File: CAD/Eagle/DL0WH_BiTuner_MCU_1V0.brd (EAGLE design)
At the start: 96.5 x 96.5 mm, 526 parts, among them Q0321 ABS07-32.768KHZ, Q1321 ABS07-32.768KHZ, Q2211 ABM3B-32.0000MHZ, Q2311 ABM3B-16.0000MHZ, T1051 MMBT2222, T1111 MMBT2222, T1121 MMBT2222, T1131 MMBT2222, U0111 STM32L4Z_144PIN_SMPS, U0521 PCAL6416APW, U0621 PCAL6416APW, U0711 IS25LP032D, U0721 IS25LP032D, U0801 CAT24C64, U0911 ZIO_EINK_1IN54, U1001 MIDAS_MCCOG21605B6W-FPTLWI, U1301 BNO085, U1401 BME680, U1501 LM4120IM5-3.0, U1511 MAX5217, U1531 CFPT-141-20MHZ, U1541 OPA354, U1542 LPV811, U1601 Si5338, U1651 TS5A23166, U1701 PCM1863, U1801 WM8523, U1901 SIM868, U2001 74LVC4245A, U2101 74LVC4245A, U2201 SX1262, U2271 PE4259, U2301 AX5243, U2401 LM53603-Q1, U2501 BQ24193, U2541 LPV811, U2601 BQ25570, U2681 TS5A23166, U2701 TPS62051, U2751 MCP4661-104E-MS, U2801 TS5A23166, U2901 TS5A23166, U3001 TS5A23166, U3101 TS5A23166, U3391 TS5A23166, U3392 TDK B4310, X1201 TTE_EN11-HSM, X1951 MICROSIM-8P_SDCARD-8P_MOLEX-1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, X2411 WIRE-TO-BOARD_5MM08_1X02, X2551 JST_S3B-XH-A, X2601 WIRE-TO-BOARD_5MM08_1X02, X3201 MOLEX 105017-0001, X3301 SMA_SMT_AMPHENOL-901-143, X3311 SAMTEC SMA-J-P-H-RA-TH1, X3371 SMA_SMT_AMPHENOL-901-143, SAM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, X3381 SMA_SMT_AMPHENOL-901-143, SAM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, X3391 SMA_SMT_AMPHENOL-901-143, SAM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, X3401 CUI SJ1-3535NS, X3411 CUI SJ1-3535NS, X3511 2X20/90_1MM27_HARWIN_M50-3202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, X3512 2X20/90_1MM27_HARWIN_M50-3202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, X3531 2X20/90_1MM27_HARWIN_M50-3202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, X3532 2X20/90_1MM27_HARWIN_M50-3202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

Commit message: HW_1V0 - CAD/Eagle - Initial setup of new PCB
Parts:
- removed C0404, C0405, C0406, C0407, C0408, C0409, C0421, C0422, C0441, C0621, C0901, C1001, C1101, C1301, C1302, C1303, C1401, C1501, C1511, C1512, C1531, C1541, C1543, C1602, C1603, C1605, C1702, C1703, C1705, C1902, C2101, C2202, C2271, C2301, C2302, C2303, C2541, C2602, C2702, C2751, C2801, C2802, C2803, C2901, C2902, C2903, C3001, C3002, C3003, C3101, C3102, C3103, C3104, C3105, C3393: 100nF, df4iah_rcl:C0402
- removed C0423, C1801, C1802, C2606: 4.7uF, df4iah_rcl:C0402
- removed C0442, C1011, C1012, C1522, C1811, C1812, C1961, C2502, C2521: 1uF, df4iah_rcl:C0402
- removed C0711, C0721, C0801, C1601, C1604, C1951, C1955: 220nF, df4iah_rcl:C0402
- removed C1201, C1202, C1203, C1542, C2272: 1nF, df4iah_rcl:C0402
- removed C1321, C1322, C1952, C1953, C1954: 22pF, df4iah_rcl:C0402
- removed C1532: 100pF, df4iah_rcl:C0402
- removed C1615, C1616, C1712, C1722, C1903, C2603, C2605, C2653: 10nF, df4iah_rcl:C0402
- removed C1701, C1704, C1711, C1721, C1904, C2201, C2501, C2504, C2505, C2511, C2601, C2652, C2701: 10uF, df4iah_rcl:C0402
- removed C1706, C1803: 2.2uF, df4iah_rcl:C0402
- removed C1831, C1841: 2.7nF, df4iah_rcl:C0402
- removed C1901, C2204: 47pF, df4iah_rcl:C0402
- removed C2203: 470nF, df4iah_rcl:C0402
- removed C2205, C2503: 47nF, df4iah_rcl:C0402
- removed C2263, C2282, C2283: 3.3pF, df4iah_rcl:C0402
- removed C2264, C2281: 39pF, df4iah_rcl:C0402
- removed C2265, C2293, C3371, C3372, C3381, C3382, C3391, C3392: 0pF, df4iah_rcl:C0402
- removed C2266: 5.6pF, df4iah_rcl:C0402
- removed C2267: 2.2pF, df4iah_rcl:C0402
- removed C2291, C3386: 1.8pF, df4iah_rcl:C0402
- removed C2292: 2.4pF, df4iah_rcl:C0402
- removed C2312, C2313, C2316: N/A, df4iah_rcl:C0402
- removed C2314, C2315: 4.3pF, df4iah_rcl:C0402
- removed C2317, C2318, C2321, C2322, C2323: 4.7pF, df4iah_rcl:C0402
- removed C2682: 1F_6V_SCMR18H105MRBB0, df4iah_rcl:C115-080X160_POL
- removed C2703: 22uF, df4iah_rcl:C0402
- removed C2791: 6.8pF, df4iah_rcl:C0402
- removed C3383: 0.5pF, df4iah_rcl:C0402
- removed C3385, C3389: 1.2pF, df4iah_rcl:C0402
- removed C3388: 1.5pF, df4iah_rcl:C0402
- removed D1101: ASMT-YTB7-0AA02_RGB, df4iah_led:ASMT-YTB7_0AA02_RGB
- removed D1901: CMAD6001, df4iah_diode:SOD923
- removed D1902: MMSZ4690-E3-08 (5.6V), df4iah_diode:SOD123
- removed D2521, D2681, D2801, D2802: CRS08, df4iah_diode:SOD80C
- removed FM1, FM2, FM3: (no value), df4iah_fiducial:FIDUCIAL_MARK_1MM
- removed L1701, L1801: 10uH, df4iah_rcl:L0603
- removed L2201: 15uH, df4iah_rcl:L_3.00MM_X_3.00MM
- removed L2261: 0R, df4iah_rcl:L0603
- removed L2262: 47nH, df4iah_rcl:L0603
- removed L2263: 2.5nH, df4iah_rcl:L0603
- removed L2264, L3386, L3388: 4.7nH, df4iah_rcl:L0603
- removed L2282: 9.1nH, df4iah_rcl:L0603
- removed L2291: 15nH, df4iah_rcl:L0603
- removed L2311, L2316, L2317, L2321: 22nH, df4iah_rcl:L0603
- removed L2312, L2313: 100nH, df4iah_rcl:L0603
- removed L2314, L2315: 43nH, df4iah_rcl:L0603
- removed L2501: 2.2uH, df4iah_rcl:L_6.00MM_X_6.00MM
- removed L2601: 22uH, df4iah_rcl:WE-TPC_3MM8-3MM8_R-1MM3
- removed L2651, L2791: 10uH, df4iah_rcl:L_4.90MM_X_4.90MM
- removed L3384: 1.2nH, df4iah_rcl:L0603
- removed L3387: 2.7nH, df4iah_rcl:L0603
- removed L3393: WE-CBF_300R, rcl:L3216C
- removed Q1321: ABS07-32.768KHZ, df4iah_crystal:ABS07
- removed Q2211: ABM3B-32.0000MHZ, df4iah_crystal:ABM3B
- removed Q2311: ABM3B-16.0000MHZ, df4iah_crystal:ABM3B
- removed R0531, R0631, R0901, R0902, R0903, R0904, R1301, R1302, R1303, R1304, R1538, R1539, R1541, R1623, R1631, R1632, R1643, R1644, R1651, R1751, R1752, R1753, R1761, R1821, R1822, R1823, R1824, R1951, R1952, R1953, R2110, R2111, R2112, R2113, R2120, R2121, R2122, R2123, R2211, R2221, R2222, R2223, R2224, R2251, R2252, R2253, R2321, R2341, R2351, R2391, R2554, R2811, R3501, R3502, R3503, R3504, R3505, R3506, R3507, R3508, R3509, R3510, R3511, R3514, R3515, R3516, R3517, R3518, R3519, R3520, R3521, R3522, R3523, R3566, R3567, R3568, R3569, R3570, R3571, R3572, R3573, R3574, R3575, R3576, R3579, R3580, R3581, R3582, R3583, R3584, R3585, R3586, R3587, R3588: 47R, df4iah_rcl:R0402
- removed R0581, R0591, R0681, R0691: 1MR, df4iah_rcl:EXBD
- removed R0621, R1521, R2331, R2332, R2612, R2701, R2711: 100kR, df4iah_rcl:R0402
- removed R0891, R0892, R1811, R1812, R2521, R2651, R2681, R3512, R3513, R3577, R3578: 0R, df4iah_rcl:R0402
- removed R1031: 220kR, df4iah_rcl:R0402
- removed R1051, R1111, R1121, R1131: 1.5kR, df4iah_rcl:R0402
- removed R1052, R1112, R1122, R1132: 2.0kR, df4iah_rcl:R0402
- removed R1053: 27R, df4iah_rcl:R0402
- removed R1113, R1123, R1133: 27R, rcl:R0805
- removed R1331, R1332: 2kR, df4iah_rcl:R0402
- removed R1531, R1711, R1721, R1901, R1942: 10kR, df4iah_rcl:R0402
- removed R1542, R2803, R2804: 1MR, df4iah_rcl:R0402
- removed R1543, R2541: 33kR, df4iah_rcl:R0402
- removed R1611, R1612, R1635, R1636, R1661, R2114, R2115, R2116, R2117, R2124, R2125, R2126, R2127: N/A, df4iah_rcl:R0402
- removed R1712, R1722, R2801, R2802: 100R, df4iah_rcl:R0402
- removed R1731, R1741, R1742, R1743, R1744, R1745, R1746: D.C., df4iah_rcl:R0402
- removed R1831, R1841: 560R, df4iah_rcl:R0402
- removed R1941: NTC 10kR, df4iah_rcl:R0402
- removed R1943, R1944: 4.7kR, df4iah_rcl:R0402
- removed R1961, R1962: 22R, df4iah_rcl:R0402
- removed R2501: 240R, df4iah_rcl:R0402
- removed R2511: 2.27kR, df4iah_rcl:R0402
- removed R2512: 6.86kR, df4iah_rcl:R0402
- removed R2611: 1kR, df4iah_rcl:R0402
- removed R2621, R2633: 1.82MR, df4iah_rcl:R0402
- removed R2622: 10.0MR, df4iah_rcl:R0402
- removed R2631: 3.65MR, df4iah_rcl:R0402
- removed R2632: 7.50MR, df4iah_rcl:R0402
- removed R2641: 4.75MR, df4iah_rcl:R0402
- removed R2642: 8.20MR, df4iah_rcl:R0402
- removed R2712: 150kR, df4iah_rcl:R0402
- removed R3371, R3381, R3391: 0R, df4iah_rcl:R0603
- removed RPOLY3393: 50mA/150mA, rcl:R1210
- removed SJ0121, SJ0421, SJ0422, SJ0423, SJ0424: (no value), df4iah_jumper:SJ
- removed T1051, T1111, T1121, T1131: MMBT2222, transistor:SOT23
- removed TP_+1V1, TP_+1V2_MCU, TP_+3V3_HICUR, TP_+3V3_XO, TP_+3V3_XO_PA, TP_BQ_VBAT, TP_BQ_VOUT, TP_BQ_VSTOR, TP_IN_CLK1, TP_IN_CLK2, TP_LIPO_BAT, TP_LIPO_CUR, TP_LIPO_SYS, TP_VSOL, TP_VUSB_SW: PTR1B1,27, testpad:B1,27
- removed TP_AX_ADC1, TP_AX_ADC2, TP_AX_IRQ, TP_AX_TCXO_EN, TP_SX_DIO1, TP_SX_DIO2, TP_SX_DIO3: PTR1TP06R, testpad:TP06R
- removed U0111: STM32L4Z_144PIN_SMPS, df4iah_stm32l4:LQFP144
- removed U0621: PCAL6416APW, df4iah_dataconvertion:TSSOP24_SOT355-1
- removed U0711, U0721: IS25LP032D, df4iah_memory:SOIC8_150MIL
- removed U0801: CAT24C64, df4iah_memory:SOIC8_150MIL
- removed U0911: ZIO_EINK_1IN54, df4iah_lcd:ZIO_EINK_1IN54
- removed U1001: MIDAS_MCCOG21605B6W-FPTLWI, df4iah_lcd:MIDAS_MCCOG21605B6W-FPTLWI
- removed U1301: BNO085, df4iah_sensors:BNO085_LGA28
- removed U1401: BME680, df4iah_sensors:BME680
- removed U1501: LM4120IM5-3.0, df4iah_powersupply:SOT95P285X120-5N
- removed U1511: MAX5217, df4iah_dac:µMAX8
- removed U1531: CFPT-141-20MHZ, df4iah_osc:CFPT-141
- removed U1541: OPA354, df4iah_opamp:SOT-23-5
- removed U1542, U2541: LPV811, df4iah_opamp:SOT-23-5
- removed U1601: Si5338, df4iah_osc:QFN24_P0MM5_CTRPAD
- removed U1651, U2681, U2801, U2901, U3001, U3101, U3391: TS5A23166, df4iah_sc-switches:R-PDSO-G8
- removed U1701: PCM1863, df4iah_adc:R-PDSO-G30
- removed U1801: WM8523, df4iah_dac:TSSOP20
- removed U1901: SIM868, df4iah_gsm:SIM868
- removed U2101: 74LVC4245A, df4iah_dataconvertion:TSSOP24_SOT355-1
- removed U2201: SX1262, df4iah_rf:QFN24-4X4-0P5-PAD
- removed U2271: PE4259, df4iah_rf:SC-70_6-LEAD_2X1MM25_0P65
- removed U2301: AX5243, df4iah_rf:QFN20-4X4-0P5-PAD
- removed U2501: BQ24193, df4iah_powersupply:VQFN-24
- removed U2601: BQ25570, df4iah_powersupply:V-PVQFN-20
- removed U2701: TPS62051, df4iah_powersupply:S-PDSO-G10
- removed U2751: MCP4661-104E-MS, df4iah_dig-pot:TSSOP14
- removed U3392: TDK B4310, df4iah_rf:QCS5P
- removed X1201: TTE_EN11-HSM, df4iah_switch:TTE_EN11-HSM
- removed X1951: MICROSIM-8P_SDCARD-8P_MOLEX-104642-1610, df4iah_connector:MICROSIM-8P_SDCARD-8P_MOLEX-104642-1610
- removed X1961: (no value), df4iah_connector:2X02
- removed X2551: JST_S3B-XH-A, df4iah_connector:JST_S3B-XH-A
- removed X2601: WIRE-TO-BOARD_5MM08_1X02, df4iah_connector:WIRE-TO-BOARD_5MM08_1X02
- removed X3371, X3381, X3391: SMA_SMT_AMPHENOL-901-143, SAMTEC SMA-J-P-H-RA-TH1, df4iah_connector:SMA_SMT_AMPHENOL_901-143
- removed X3401, X3411: CUI SJ1-3535NS, df4iah_connector:SJ1-353XNS_3MM5-STEREO-AUDIO-JACKS
- removed X3511, X3512, X3531, X3532: 2X20/90_1MM27_HARWIN_M50-3202045_SOCKET, df4iah_connector:2X20/90_1MM27_HARWIN_M50-3202045_SOCKET
- added C9801, C9802, C9803, C9804, C9805, C9901, C9902, C9903, C9904, C9905: 1uF, rcl:C0805
- added H3651, H3661: MOUNT-PAD-ROUND3.0, df4iah_holes:3,0-PAD
- added R9801, R9802, R9803, R9804, R9901, R9902, R9903, R9904: 47R, df4iah_rcl:R0603
- added U0101: STM32L476RXT_64PIN_LDO, df4iah_stm32l4:LQFP64
- added U9801, U9901: MAX232_SOIC16, df4iah_dataconvertion:SOIC16N
- added X9701, X9702: (no value), df4iah_connector:2X10
- added X9851, X9852, X9853, X9951, X9952, X9953: WIRE-TO-BOARD_5MM08_1X02, df4iah_connector:WIRE-TO-BOARD_5MM08_1X02
- C0451: value 1F_6V_SCMR18H105MRBB0 -> 47uF; device df4iah_rcl:C115-080X160_POL -> df4iah_rcl:C0805
- H3611, H3621, H3631: value MOUNT-PAD-ROUND2.8 -> MOUNT-PAD-ROUND3.0; device holes:2,8-PAD -> df4iah_holes:3,0-PAD
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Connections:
- removed net +1V2: C2703.1, C2791.2, C3101.1, L2791.1, TP_+1V1.TP, U2751.8, U3101.1, U3101.5
- removed net +1V5_UNUSED: SJ0424.2
- removed net +1V8_UNUSED: SJ0423.2
- removed net +2V5_UNUSED: SJ0422.2
- removed net +3V0_20MHZ_VCTCXO: C1511.1, C1531.1, U1501.5, U1511.1, U1531.4
- removed net +3V3_GPS: RPOLY3393.1, U3391.2, U3391.6
- removed net +3V3_HICUR: C1601.1, C1602.1, C1603.1, C1604.1, C1605.2, C1701.1, C1702.1, C1801.1, C3003.1, L1701.2, L1801.2, TP_+3V3_HICUR.TP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
- removed net +3V3_XO: C1501.1, C1512.1, C2903.1, TP_+3V3_XO.TP, U1501.3, U1501.4, U1511.5, U1511.7, U2901.6
- removed net +3V3_XO_PA: C1541.1, TP_+3V3_XO_PA.TP, U1541.5, U2901.2
- removed net +5V0: C2521.2, D2521.C, R2521.2, R2681.2, U2501.1, U2501.24, X3511.37, X3511.38, X3531.37, X3531.38
- removed net 20MHZ_DAC_OUT: R1521.1, U1511.6
- removed net 20MHZ_XO: R1538.1, U1531.3, U1541.3
- removed net 20MHZ_XON: C1616.1, R1539.2, R1661.1
- removed net 20MHZ_XOP: C1615.1, R1538.2, R1661.2
- removed net AD_VCTCXO1: R1543.1, U1542.1, U1542.4
- removed net AUDIOADC_AVDD: C1703.2, L1701.1, U1701.8
- removed net AUDIOADC_BCK: R1752.1, U1701.17
- removed net AUDIOADC_DOUT: R1751.1, U1701.18
- removed net AUDIOADC_INTA: R1761.1, U1701.21
- removed net AUDIOADC_LDO: C1704.1, C1705.1, U1701.11
- removed net AUDIOADC_LRCK: R1753.1, U1701.16
- removed net AUDIOADC_MIC_BIAS: R1731.2, U1701.5
- removed net AUDIOADC_VINL1: C1712.1, R1712.2, U1701.3
- removed net AUDIOADC_VINL1_R: C1711.2, R1712.1
- removed net AUDIOADC_VINL2: R1741.2, U1701.1
- removed net AUDIOADC_VINL3: R1743.2, U1701.29
- removed net AUDIOADC_VINL4: R1745.2, U1701.27
- removed net AUDIOADC_VINR1: C1722.1, R1722.2, U1701.4
- removed net AUDIOADC_VINR1_R: C1721.2, R1722.1
- removed net AUDIOADC_VINR2: R1742.2, U1701.2
- removed net AUDIOADC_VINR3: R1744.2, U1701.30
- removed net AUDIOADC_VINR4: R1746.2, U1701.28
- removed net AUDIOADC_VREF: C1706.1, U1701.6
- removed net AUDIO_DAC_A0: R1811.2, U1801.15
- removed net AUDIO_DAC_A1: R1812.2, U1801.12
- removed net AUDIO_DAC_AVDD: C1802.2, L1801.1, U1801.19
- removed net AUDIO_DAC_BCLK: R1822.2, U1801.10
- removed net AUDIO_DAC_CPCA: C1811.1, U1801.5
- removed net AUDIO_DAC_CPCB: C1811.2, U1801.3
- removed net AUDIO_DAC_CPVOUTN: C1812.2, U1801.2
- removed net AUDIO_DAC_DACDAT: R1821.2, U1801.8
- removed net AUDIO_DAC_LINEVOUTL: R1831.1, U1801.1
- removed net AUDIO_DAC_LINEVOUTR: R1841.1, U1801.20
- removed net AUDIO_DAC_LRCLK: R1823.2, U1801.9
- removed net AUDIO_DAC_MCLK: R1824.2, U1801.11
- removed net AUDIO_DAC_VMID: C1803.2, U1801.18
- removed net AUDIO_IN_L: C1711.1, R1711.2, X3401.12, X3401.22
- removed net AUDIO_IN_R: C1721.1, R1721.2, X3401.13, X3401.23
- removed net AUDIO_OUT_L: C1831.1, R1831.2, X3411.12, X3411.22
- removed net AUDIO_OUT_R: C1841.1, R1841.2, X3411.13, X3411.23
- removed net AX_8MHZ: R2321.2, U1601.4
- removed net AX_ADC1: R2331.1, TP_AX_ADC1.TP, U2301.17
- removed net AX_ADC2: R2332.1, TP_AX_ADC2.TP, U2301.18
- removed net AX_ANTN: C2313.1, C2315.1, L2313.1, U2301.4
- removed net AX_ANTP: C2312.1, C2314.1, L2312.1, U2301.3
- removed net AX_B1: C2317.1, L2314.2, L2317.1
- removed net AX_B2: C2316.1, C2318.1, L2315.2, L2316.2
- removed net AX_CLK16A: Q2311.1, U2301.20
- removed net AX_CLK16B: Q2311.3, U2301.19
- removed net AX_COMB: C2318.2, C2321.1, C2322.1, L2317.2, L2321.1
- removed net AX_IRQ: R2351.2, TP_AX_IRQ.TP, U2301.14
- removed net AX_L1: L2311.1, U2301.8
- removed net AX_L2: L2311.2, U2301.7
- removed net AX_SYSCLK: R2321.1, U2301.9
- removed net AX_T1: C2314.2, L2314.1
- removed net AX_T2: C2315.2, L2315.1
- removed net AX_VDD1: C2302.2, U2301.1
- removed net AX_VDD5: C2303.2, U2301.5
- removed net BNO085_CAP: C1303.1, U1301.9
- removed net BNO085_CLKSEL1_XOUT32: C1322.1, Q1321.1, U1301.26
- removed net BNO085_ENV_SCL: R1332.1, U1301.15
- removed net BNO085_ENV_SDA: R1331.1, U1301.16
- removed net BNO085_H_CSN: R1304.2, U1301.18
- removed net BNO085_INTN: R1302.2, U1301.14
- removed net BNO085_MISO: R1301.2, U1301.20
- removed net BNO085_PS0_WAKE: R1303.2, U1301.6
- removed net BNO085_XIN32: C1321.1, Q1321.2, U1301.27
- removed net BQ_LBOOST: L2601.1, R2612.2, U2601.20
- removed net BQ_LBUCK: L2651.2, U2601.16
- removed net BQ_OK_HYST: R2632.2, R2633.1, U2601.10
- removed net BQ_OK_PROG: R2631.2, R2632.1, U2601.11
- removed net BQ_VBAT: C2682.+, TP_BQ_VBAT.TP, U2601.18, U2681.8
- removed net BQ_VBAT_OV: R2621.2, R2622.1, U2601.7
- removed net BQ_VOUT: C2652.1, C2653.1, L2651.1, R2651.1, TP_BQ_VOUT.TP, U2601.14
- removed net BQ_VOUT_SET: R2641.2, R2642.1, U2601.12
- removed net BQ_VRDIFF: R2622.2, R2633.2, R2642.2, U2601.8
- removed net BQ_VREF_SAMP: C2603.2, U2601.4
- removed net BQ_VSTOR: C2605.1, C2606.1, D2681.C, TP_BQ_VSTOR.TP, U2601.19, U2601.3, U2601.6, U2681.2, U2681.3, U2681.6, U2681.7
- removed net BQ_VSTOR_SW: D2681.A, R2681.1, U2681.1, U2681.5
- removed net BT_ANT: C3382.1, R3381.2, X3381.1
- removed net CH1_ANT: C2283.2, L2282.1, X3301.1
- removed net CH2_ANT: C2321.2, C2323.1, L2321.2, X3311.1
- removed net CLK0_N: R1643.2, X3532.4
- removed net CLK0_P: R1644.2, X3532.3
- removed net CLK2_N: R1631.2, X3512.4
- removed net CLK2_P: R1632.2, X3512.3
- removed net CLK_AUDIO_ADC: R1623.1, U1701.15
- removed net EINK_BUSY_R: R0904.2, U0911.8
- removed net EINK_CS_R: R0901.2, U0911.5
- removed net EINK_D/C_R: R0902.2, U0911.6
- removed net EINK_RESET_R: R0903.2, U0911.7
- removed net EVT_N_OUT: R3509.2, X3511.29
- removed net EVT_S_OUT: R3574.2, X3531.29
- removed net GPS_ANT: C3392.1, R3391.2, X3391.1
- removed net GPS_ANT_SAW: C3391.1, L3393.1, R3391.1, U3392.4
- removed net GPS_POLY: L3393.2, RPOLY3393.2
- removed net GSM_ANT: C3372.1, R3371.2, X3371.1
- removed net I2C1_SCL: R0612.1, R0891.1, U0521.22, U0621.22, U0801.6, U1001.7, U1401.4, U1511.3, U1601.12, U1701.24, U1801.14, U2501.5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
- removed net I2C1_SDA: R0611.1, R0892.1, U0521.23, U0621.23, U0801.5, U1001.6, U1401.3, U1511.4, U1601.19, U1701.23, U1801.13, U2501.6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
- removed net I2C2_SCL_N: R3512.2, X3512.7
- removed net I2C2_SCL_S: R3577.2, X3532.7
- removed net I2C2_SDA_N: R3513.2, X3512.8
- removed net I2C2_SDA_S: R3578.2, X3532.8
- removed net I2S_FS_N_IN: R3523.2, X3512.26
- removed net I2S_FS_N_OUT: R3520.2, X3512.20
- removed net I2S_FS_S_IN: R3588.2, X3532.26
- removed net I2S_FS_S_OUT: R3585.2, X3532.20
- removed net I2S_MCLK_N_OUT: R3519.2, X3512.19
- removed net I2S_MCLK_S_OUT: R3584.2, X3532.19
- removed net I2S_SCK_N_IN: R3521.2, X3512.23
- removed net I2S_SCK_N_OUT: R3517.2, X3512.17
- removed net I2S_SCK_S_IN: R3586.2, X3532.23
- removed net I2S_SCK_S_OUT: R3582.2, X3532.17
- removed net I2S_SD_N_IN: R3522.2, X3512.24
- removed net I2S_SD_N_OUT: R3518.2, X3512.18
- removed net I2S_SD_S_IN: R3587.2, X3532.24
- removed net I2S_SD_S_OUT: R3583.2, X3532.18
- removed net LCD_BL_K: T1051.3, U1001.11
- removed net LCD_CAP1N: C1011.2, U1001.2
- removed net LCD_CAP1P: C1011.1, U1001.3
- removed net LCD_VOUT: C1012.1, U1001.1
- removed net LED_B_B: R1051.2, R1052.1, T1051.1
- removed net LED_B_B1: R1131.2, R1132.1, T1131.1
- removed net LED_B_E: R1053.2, T1051.2
- removed net LED_B_E1: R1133.2, T1131.2
- removed net LED_B_K1: D1101.1, T1131.3
- removed net LED_G_B1: R1121.2, R1122.1, T1121.1
- removed net LED_G_E1: R1123.2, T1121.2
- removed net LED_G_K1: D1101.2, T1121.3
- removed net LED_R_B1: R1111.2, R1112.1, T1111.1
- removed net LED_R_E1: R1113.2, T1111.2
- removed net LED_R_K1: D1101.3, T1111.3
- removed net LIPO_ADC_CUR_IN_LOOP: R2541.2, U2541.1, U2541.4
- removed net LIPO_BAT: C2511.1, TP_LIPO_BAT.TP, U2501.13, U2501.14, X2551.1
- removed net LIPO_BTST: C2503.1, U2501.21
- removed net LIPO_ILIM: R2501.2, U2501.10, U2541.3
- removed net LIPO_INT: R2554.2, U2501.7
- removed net LIPO_PMID: C2501.1, U2501.23
- removed net LIPO_REGN: C2502.1, R2511.2, U2501.22
- removed net LIPO_SW: C2503.2, L2501.2, U2501.19, U2501.20
- removed net LIPO_SYS: C1901.2, C1902.2, C1904.2, C2504.1, C2505.1, D1902.C, L2501.1, TP_LIPO_SYS.TP, U1901.34, U1901.35, U2501.15, U2501.16
- removed net LIPO_TS12: R2511.1, R2512.1, U2501.11, U2501.12, X2551.2
- removed net LS2_B12: R2124.1, U2101.17
- removed net LS2_B13: R2125.1, U2101.16
- removed net LS2_B14: R2126.1, U2101.15
- removed net LS2_B15: R2127.1, U2101.14
- removed net LS2_B4: R2114.2, U2101.7
- removed net LS2_B4_R: R2124.2
- removed net LS2_B5: R2115.2, U2101.8
- removed net LS2_B5_R: R2125.2
- removed net LS2_B6: R2116.2, U2101.9
- removed net LS2_B6_R: R2126.2
- removed net LS2_B7: R2117.2, U2101.10
- removed net LS2_B7_R: R2127.2
- removed net MCP4661_P0B_P1W: U2751.10, U2751.6
- removed net MCU_AX_MISO: R2341.2, U2301.12
- removed net MCU_AX_SEL_OUT: R2391.2, U2301.10
- removed net MCU_HSE_R: R1651.2, U1651.2, U1651.5
- removed net MCU_RF_SYNC_IN_R: R2113.2, U2101.6
- removed net MCU_SPI3_MOSI: R2223.2, U0911.3, U1301.17, U2201.17, U2301.13
- removed net MCU_SPI3_SCK: R2222.2, U0911.4, U1301.19, U2201.18, U2301.11
- removed net MCU_SX_SEL_OUT: R2221.2, U2201.19
- removed net MCU_VBUS_SOFT_SW_EN_OUT_R: R2803.1, R2811.2, U2801.7
- removed net MCU_VDD12: C3103.1, C3104.2, C3105.1, TP_+1V2_MCU.TP, U0111.142, U0111.70, U3101.2, U3101.6
- removed net MCU_VDDIO2: C0421.2, C0422.1, C0423.1, SJ0421.1, SJ0422.1, SJ0423.1, SJ0424.1, U0111.131, U0111.95
- removed net MCU_VREF_P: C0441.2, C0442.2, U0111.32
- removed net MCU_VSSA: SJ0121.2, U0111.30
- removed net MC_SW: X1951.SW
- removed net PD0: U0111.114
- removed net PD1: R3516.1, R3581.1, U0111.115
- removed net PD10: R3567.1, U0111.79
- removed net PD11: R1751.2, R3522.1, R3587.1, U0111.80
- removed net PD12: R1753.2, R3523.1, R3588.1, U0111.81
- removed net PD13: U0111.82
- removed net PD14: R3568.1, U0111.85
- removed net PD15: R3569.1, U0111.86
- removed net PD3: R3515.1, R3580.1, U0111.117
- removed net PD4: U0111.118
- removed net PD5: U0111.119
- removed net PD6: U0111.122
- removed net PD7: U0111.123, U0721.7
- removed net PD8: R2211.1, U0111.77
- removed net PD9: R3566.1, U0111.78
- removed net PE0: U0111.140
- removed net PE1: U0111.141
- removed net PE10: R1824.1, R3519.1, R3584.1, U0111.63
- removed net PE11: U0111.64, U0711.1, U0721.1
- removed net PE12: U0111.65, U0711.5
- removed net PE13: U0111.66, U0711.2
- removed net PE14: U0111.67, U0711.3
- removed net PE15: U0111.68, U0711.7
- removed net PE2: U0111.1
- removed net PE3: R1821.1, R3518.1, R3583.1, U0111.2
- removed net PE4: U0111.3
- removed net PE5: U0111.4
- removed net PE6: R1052.2, U0111.5
- removed net PE7: R2351.1, U0111.58
- removed net PE8: R1822.1, R3517.1, R3582.1, U0111.59
- removed net PE9: R1823.1, R3520.1, R3585.1, U0111.60
- removed net PEXPA_INTN: R0531.2, U0521.1
- removed net PEXPB_INTN: R0631.2, U0621.1
- removed net PEXPB_P0_0_R: R0681.2, U0621.4, U2701.4
- removed net PEXPB_P0_1_R: R0681.3, U0621.5, U2701.2
- removed net PEXPB_P0_2_R: R0681.4, U0621.6, U2501.4
- removed net PEXPB_P0_3_R: R0681.5, U0621.7, U2501.3
- removed net PEXPB_P0_4_R: R0681.7, U0621.8, U1801.7
- removed net PEXPB_P0_5_R: R0681.8, TP_AX_TCXO_EN.TP, U0621.9, U2301.15
- removed net PEXPB_P0_6_R: R0681.9, U0621.10
- removed net PEXPB_P0_7_R: R0681.10, U0621.11, U3391.3, U3391.7
- removed net PEXPB_P1_0: R2121.1, U2101.20
- removed net PEXPB_P1_0_R: R0691.2, R2121.2, U0621.13
- removed net PEXPB_P1_1: R2110.2, U2101.3
- removed net PEXPB_P1_1_R: R0691.3, R2110.1, U0621.14
- removed net PEXPB_P1_2: R2112.2, U2101.5
- removed net PEXPB_P1_2_R: R0691.4, R2112.1, U0621.15
- removed net PEXPB_P1_3_R: R0691.5, R0903.1, U0621.16
- removed net PEXPB_P1_4_R: R0691.7, U0621.17
- removed net PEXPB_P1_5_R: C1201.1, R0691.8, U0621.18, X1201.A
- removed net PEXPB_P1_6_R: C1202.1, R0691.9, U0621.19, X1201.B
- removed net PEXPB_P1_7_R: C1203.1, R0691.10, U0621.20, X1201.E
- removed net PEXPB_RESET: R0621.1, U0621.3
- removed net PE_RFC: C2281.1, U2271.5
- removed net PE_RFC_2: C2281.2, C2282.2, L2282.2
- removed net PF0: R3513.1, R3578.1, U0111.10
- removed net PF1: R3512.1, R3577.1, U0111.11
- removed net PF10: U0111.22, U0711.6, U0721.6
- removed net PF11: R1304.1, U0111.49
- removed net PF12: C2272.1, R2252.2, U0111.50, U2271.4
- removed net PF13: R1302.1, U0111.53
- removed net PF14: R2391.1, U0111.54
- removed net PF15: R2221.1, U0111.55
- removed net PF2: U0111.12
- removed net PF3: R0531.1, U0111.13
- removed net PF4: R0631.1, U0111.14
- removed net PF5: R2811.1, U0111.15
- removed net PF6: R3510.1, U0111.18
- removed net PF7: R2612.1, U0111.19
- removed net PF8: R3575.1, U0111.20
- removed net PF9: R2027.2, U0111.21
- removed net PG0: R2253.2, U0111.56
- removed net PG1: R2251.2, U0111.57
- removed net PG10: R3506.1, R3571.1, U0111.125
- removed net PG11: R3508.1, R3573.1, U0111.126
- removed net PG12: R3507.1, R3572.1, U0111.127
- removed net PG13: R0892.2, U0111.128
- removed net PG14: R0891.2, U0111.129
- removed net PG2: U0111.87
- removed net PG3: R0901.1, U0111.88
- removed net PG4: R3509.1, R3574.1, U0111.89
- removed net PG5: R0902.1, U0111.90
- removed net PG6: R2025.2, U0111.91
- removed net PG7: R2014.1, U0111.92
- removed net PG8: R2021.2, U0111.93
- removed net PG9: R3505.1, R3570.1, U0111.124
- removed net PN00: R3501.2, X3511.7
- removed net PN01: R3502.2, X3511.9
- removed net PN02: R3503.2, X3511.11
- removed net PN03: R3504.2, X3511.13
- removed net PS00: R3566.2, X3531.7
- removed net PS01: R3567.2, X3531.9
- removed net PS02: R3568.2, X3531.11
- removed net PS03: R3569.2, X3531.13
- removed net S6: X1951.S6
- removed net SC_2: R1951.2, X1951.S2
- removed net SC_3: R1952.2, X1951.S3
- removed net SC_7: R1953.1, X1951.S7
- removed net SI5338_CLK0A: R1644.1, U1601.22
- removed net SI5338_CLK0B: R1643.1, U1601.21
- removed net SI5338_CLK1A: R1636.1, U1601.18
- removed net SI5338_CLK1B: R1635.1, U1601.17
- removed net SI5338_CLK2A: R1632.1, U1601.14
- removed net SI5338_CLK2B: R1631.1, U1601.13
- removed net SI5338_CLK3A: U1601.10, U1651.1
- removed net SI5338_CLK3B: R1623.2, U1601.9
- removed net SI5338_IN5: C1615.2, U1601.5
- removed net SI5338_IN6: C1616.2, U1601.6
- removed net SI5338_IN_CLK1: R1611.1
- removed net SI5338_IN_CLK1_R: R1611.2, TP_IN_CLK1.TP, U1601.1
- removed net SI5338_IN_CLK2: R1612.1
- removed net SI5338_IN_CLK2_R: R1612.2, TP_IN_CLK2.TP, U1601.2
- removed net SI5338_OUT_CLK1_N: R1635.2
- removed net SI5338_OUT_CLK1_P: R1636.2
- removed net SIM_!PWRKEY: R2111.1, U1901.39
- removed net SIM_1PPS: R2017.1, U1901.60
- removed net SIM_ADC: R1941.2, R1942.1, U1901.38
- removed net SIM_BT_ANT: C3383.1, L3384.1, U1901.20
- removed net SIM_BT_ANT_L: C3385.1, L3384.2, L3386.1, L3387.1
- removed net SIM_BT_ANT_L_L: C3381.1, C3388.1, C3389.1, L3387.2, R3381.1
- removed net SIM_BT_ANT_L_LC: C3386.1, L3386.2
- removed net SIM_BT_ANT_L_L_LC: C3388.2, L3388.1
- removed net SIM_GNSS_EN: R1901.2, U1901.59
- removed net SIM_GPIO1: R1901.1, U1901.57
- removed net SIM_GPIO2: U1901.58
- removed net SIM_GPS_ANT: U1901.68, U3392.1
- removed net SIM_GPS_RXD: U1901.22, U1901.62
- removed net SIM_GPS_TXD: U1901.23, U1901.61
- removed net SIM_GSM_ANT: C3371.1, R3371.1, U1901.32
- removed net SIM_MCCA0: U1901.49, X1951.T7
- removed net SIM_MCCA1: U1901.48, X1951.T8
- removed net SIM_MCCA2: U1901.47, X1951.T1
- removed net SIM_MCCA3: U1901.46, X1951.T2
- removed net SIM_MCCCK: U1901.50, X1951.T5
- removed net SIM_MCCM0: U1901.51, X1951.T3
- removed net SIM_MICN: U1901.10
- removed net SIM_MICP: U1901.9
- removed net SIM_NETLIGHT: R2122.2, U1901.41
- removed net SIM_NETLIGHT_R: R2122.1, U2101.19
- removed net SIM_PWRKEY_R: R2111.2, U2101.4
- removed net SIM_RF_SYNC: R2123.2, U1901.29
- removed net SIM_RF_SYNC_R: R2123.1, U2101.18
- removed net SIM_SCL: R1944.1, U1901.65
- removed net SIM_SDA: R1943.1, U1901.64
- removed net SIM_SIM1_CLK: C1953.2, R1952.1, U1901.16
- removed net SIM_SIM1_DATA: C1954.2, R1953.2, U1901.15
- removed net SIM_SIM1_DET: U1901.14
- removed net SIM_SIM1_RST: C1952.2, R1951.1, U1901.17
- removed net SIM_SIM1_VDD: C1951.1, U1901.18, X1951.S1
- removed net SIM_SIM2_CLK: U1901.54
- removed net SIM_SIM2_DATA: U1901.53
- removed net SIM_SIM2_DET: U1901.52
- removed net SIM_SIM2_RST: U1901.55
- removed net SIM_SIM2_VDD: U1901.56
- removed net SIM_SPK1N: U1901.12
- removed net SIM_SPK1P: U1901.11
- removed net SIM_SPK2N: U1901.43
- removed net SIM_SPK2P: U1901.44
- removed net SIM_STATUS: R2120.2, U1901.42
- removed net SIM_STATUS_R: R2120.1, U2101.21
- removed net SIM_UART1_CTS: R2013.1, U1901.4
- removed net SIM_UART1_DCD: R2016.1, U1901.5
- removed net SIM_UART1_DTR: R2024.2, U1901.6
- removed net SIM_UART1_RI: R2015.1, U1901.7
- removed net SIM_UART1_RTS: R2022.2, U1901.3
- removed net SIM_UART1_RXD: R2020.2, U1901.2
- removed net SIM_UART1_TXD: R2011.1, U1901.1
- removed net SIM_USBCON_DM: R1961.2, X1961.4
- removed net SIM_USBCON_DP: R1962.2, X1961.2
- removed net SIM_USB_DM: R1961.1, U1901.26
- removed net SIM_USB_DP: R1962.1, U1901.25
- removed net SIM_USB_VBUS: C1961.2, U1901.24, X1961.3
- removed net SIM_VRTC: C1903.2, D1901.C, U1901.28
- removed net SPI2_MISO_N: R3515.2, X3512.12
- removed net SPI2_MISO_S: R3580.2, X3532.12
- removed net SPI2_MOSI_N: R3514.2, X3512.11
- removed net SPI2_MOSI_S: R3579.2, X3532.11
- removed net SPI2_SCK_N: R3516.2, X3512.13
- removed net SPI2_SCK_S: R3581.2, X3532.13
- removed net SX_BUSY: R2211.2, U2201.14
- removed net SX_DCC_SW: L2201.1, U2201.9
- removed net SX_DIO1: R2253.1, TP_SX_DIO1.TP, U2201.13
- removed net SX_DIO2: R2252.1, TP_SX_DIO2.TP, U2201.12
- removed net SX_DIO3: R2251.1, TP_SX_DIO3.TP, U2201.6
- removed net SX_MISO: R2224.2, U2201.16
- removed net SX_RFI_2: C2292.2, C2293.2, U2271.3
- removed net SX_RFI_N: C2292.1, L2291.1, U2201.22
- removed net SX_RFI_P: C2291.2, L2291.2, U2201.21
- removed net SX_RFO: L2261.2, U2201.23
- removed net SX_RFO_2: C2263.1, C2265.2, L2261.1, L2262.1, L2263.2
- removed net SX_RFO_3: C2263.2, C2264.1, C2266.1, L2263.1
- removed net SX_RFO_4: C2264.2, L2264.2
- removed net SX_RFO_5: C2267.1, L2264.1, U2271.1
- removed net SX_VREG: C2203.1, L2201.2, U2201.7
- removed net SX_VR_PA: C2204.1, C2205.1, L2262.2, U2201.24
- removed net SX_XTA: Q2211.1, U2201.3
- removed net SX_XTB: Q2211.3, U2201.4
- removed net TIMCAP_N_IN: R3510.2, X3511.31
- removed net TIMCAP_S_IN: R3575.2, X3531.31
- removed net U3311_B4_R: R2114.1
- removed net U3311_B5_R: R2115.1
- removed net U3311_B6_R: R2116.1
- removed net U3311_B7_R: R2117.1
- removed net UART1_CTS_N_IN: R3508.2, X3511.26
- removed net UART1_CTS_S_IN: R3573.2, X3531.26
- removed net UART1_RTS_N_OUT: R3507.2, X3511.25
- removed net UART1_RTS_S_OUT: R3572.2, X3531.25
- removed net UART1_RX_N_IN: R3506.2, X3511.24
- removed net UART1_RX_S_IN: R3571.2, X3531.24
- removed net UART1_TX_N_OUT: R3505.2, X3511.23
- removed net UART1_TX_S_OUT: R3570.2, X3531.23
- removed net VCTCXO_PA_N: C1542.1, R1542.1, U1541.4
- removed net VCTCXO_PA_O: R1541.1, R1542.2, U1541.1
- removed net VDD12_EN: R2701.2, U2701.8
- removed net VDD12_FB: C2791.1, U2701.5, U2751.9
- removed net VDD12_LBI: R2711.2, R2712.1, U2701.6
- removed net VDD12_SW: L2791.2, U2701.9
- removed net VDDUSB_DK: C2802.1, D2801.C, D2802.C, R2801.2, R2802.2, R2803.2, U2801.8
- removed net VDDUSB_SOFT: R2801.1, R2802.1, U2801.1
- removed net VSOL: C2601.1, C2602.1, L2601.2, R2611.1, TP_VSOL.TP, U2601.2, X2601.1
- removed net VUSB_SW: C2803.1, D2802.A, R2521.1, TP_VUSB_SW.TP, U2801.2, U2801.6
- removed net WAKEUP_N_IN: R3511.2, X3511.33
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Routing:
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- removed copper zone on layer 2, net BME680_LAYER02_CUTOUT
- removed copper zone on layer 15, net BME680_LAYER15_CUTOUT
- removed copper zone on layer 15, net POLY_BT_1
- removed copper zone on layer 2, net POLY_BT_2
- removed copper zone on layer 15, net POLY_GPS_0
- removed copper zone on layer 15, net POLY_GPS_1
- removed copper zone on layer 2, net POLY_GPS_2
- removed copper zone on layer 1, net POLY_GPS_3
- removed copper zone on layer 1, net POLY_GPS_4
- removed copper zone on layer 15, net POLY_GSM_1
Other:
- board size 96.5 x 96.5 mm -> 96.5 x 73 mm
- board text added: "CAT Ifc."
- board text added: "CTS"
- board text added: "DL0WH BiTuner V1.0 (C) 2019"
- board text added: "FWD"
- board text added: "GND"
- board text added: "REL1..20"
- board text added: "REL21..36, 12V"
- board text added: "REV"
- board text added: "RS232"
- board text added: "RTR"
- board text added: "RXD"
- board text added: "TXD"
- board text added: "USB"
- board text removed: "ADC1"
- board text removed: "ADC2"
- board text removed: "BAT"
- board text removed: "BT"
- board text removed: "C1"
- board text removed: "C2"
- board text removed: "CUR"
- board text removed: "D1"
- board text removed: "D2"
- board text removed: "D3"
- board text removed: "GPIO"
- board text removed: "GPS"
- board text removed: "GSM"
- board text removed: "HFT-Core-Module V1.1 (C) 2018 by Fakultät N, Hochschule Mannheim, Germany."
- board text removed: "HICUR"
- board text removed: "IN"
- board text removed: "IRQ"
- board text removed: "LiPo"
- board text removed: "OUT"
- board text removed: "PMIC_1V2"
- board text removed: "SIM USB"
- board text removed: "SIM-Card"
- board text removed: "SMPS"
- board text removed: "SOLAR"
- board text removed: "SYS"
- board text removed: "USW"
- board text removed: "VBAT"
- board text removed: "VBKUP"
- board text removed: "VOUT"
- board text removed: "VSOL"
- board text removed: "VSTOR"
- board text removed: "XO"
- board text removed: "XO_PA"

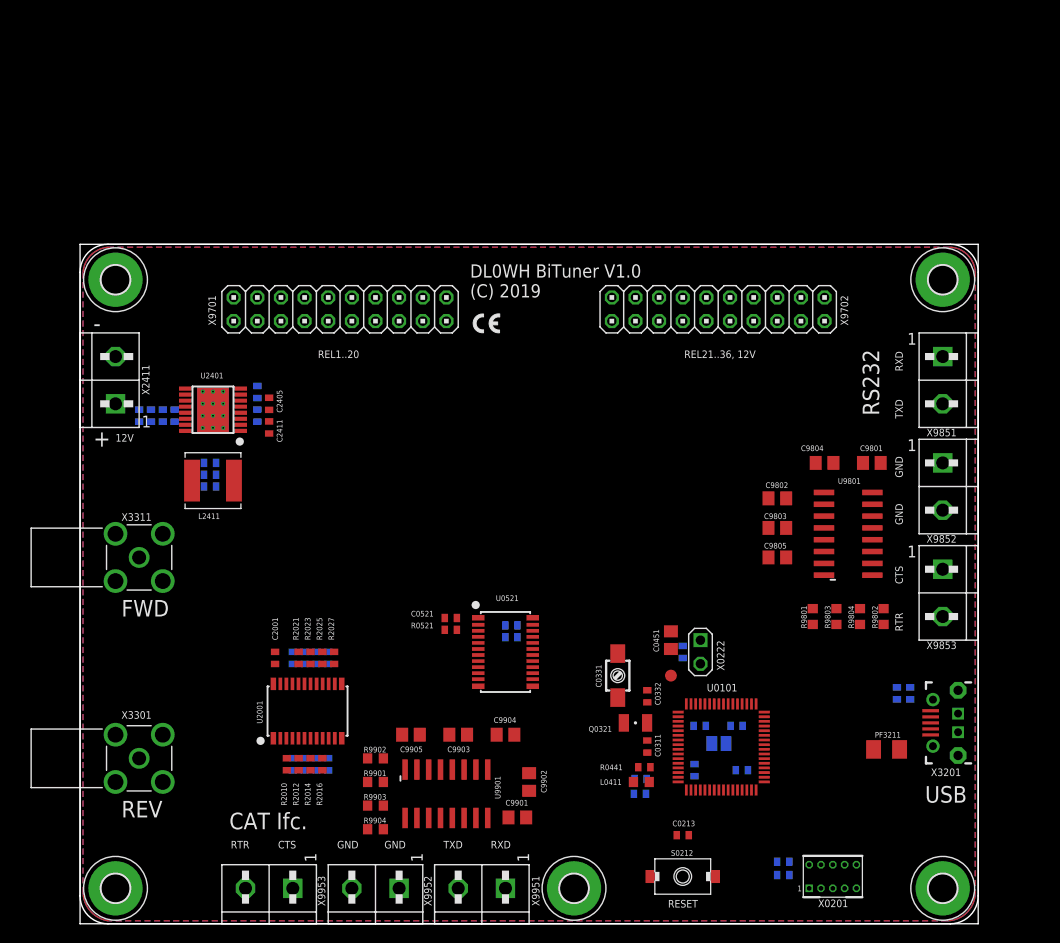
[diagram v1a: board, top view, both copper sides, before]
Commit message: HW_1V0 - CAD/Eagle - I/O drivers added
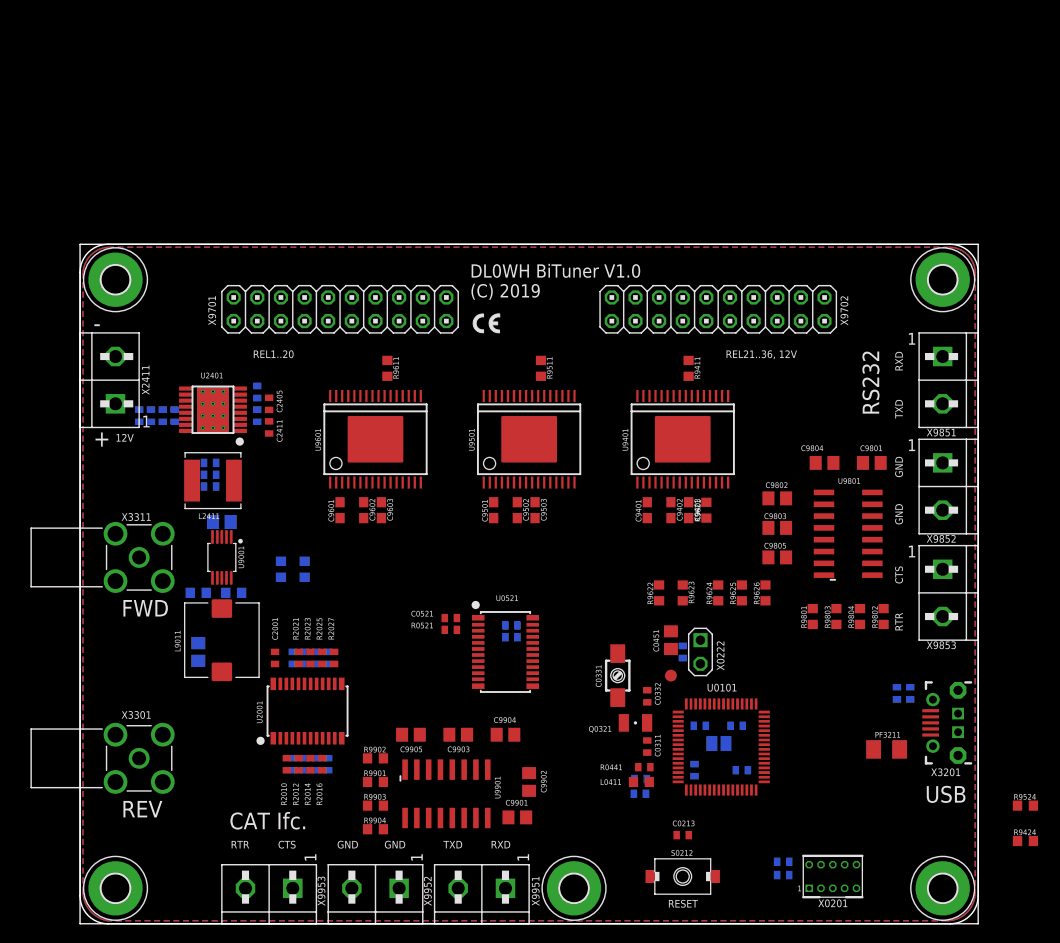
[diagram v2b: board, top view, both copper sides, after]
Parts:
- added C9001, C9011: 22uF, df4iah_rcl:C0805
- added C9401, C9402, C9501, C9502, C9601, C9602: 100nF, df4iah_rcl:C0603
- added C9403, C9503, C9603: 22uF, df4iah_rcl:C0603
- added L9011: 10uH, df4iah_rcl:L_8.00MM_X_8.00MM
- added R9001: 100kR, df4iah_rcl:R0603
- added R9002: 220kR, df4iah_rcl:R0603
- added R9021, R9022: 1MR, df4iah_rcl:R0603
- added R9411, R9424, R9511, R9524, R9611, R9621, R9623, R9624, R9625, R9626: 47R, df4iah_rcl:R0603
- added R9622: 0R, df4iah_rcl:R0603
- added U9001: TPS62051, df4iah_powersupply:S-PDSO-G10
- added U9401, U9501, U9601: MC33996, df4iah_dataconvertion:SOICW32
- turned C2421 to 180 degrees
- turned C2422 to 180 degrees
- turned C2423 to 180 degrees
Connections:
- removed net POW_IN_5V0: C2421.1, C2422.1, C2423.1, L2411.1, R2411.2, U2401.9
- removed net RELAIS1: X9701.1
- removed net RELAIS10: X9701.10
- removed net RELAIS11: X9701.11
- removed net RELAIS12: X9701.12
- removed net RELAIS13: X9701.13
- removed net RELAIS14: X9701.14
- removed net RELAIS15: X9701.15
- removed net RELAIS16: X9701.16
- removed net RELAIS17: X9701.17
- removed net RELAIS18: X9701.18
- removed net RELAIS19: X9701.19
- removed net RELAIS2: X9701.2
- removed net RELAIS20: X9701.20
- removed net RELAIS21: X9702.1
- removed net RELAIS22: X9702.2
- removed net RELAIS23: X9702.3
- removed net RELAIS24: X9702.4
- removed net RELAIS25: X9702.5
- removed net RELAIS26: X9702.6
- removed net RELAIS27: X9702.7
- removed net RELAIS28: X9702.8
- removed net RELAIS29: X9702.9
- removed net RELAIS3: X9701.3
- removed net RELAIS30: X9702.10
- removed net RELAIS31: X9702.11
- removed net RELAIS32: X9702.12
- removed net RELAIS33: X9702.13
- removed net RELAIS34: X9702.14
- removed net RELAIS35: X9702.15
- removed net RELAIS36: X9702.16
- removed net RELAIS4: X9701.4
- removed net RELAIS5: X9701.5
- removed net RELAIS6: X9701.6
- removed net RELAIS7: X9701.7
- removed net RELAIS8: X9701.8
- removed net RELAIS9: X9701.9
- new net +5V0: C2421.1, C2422.1, C2423.1, C9001.1, L2411.1, R2411.2, R9002.2, U2401.9, U9001.1, U9001.8
- new net DRV_OUT_3_10: U9401.20
- new net DRV_OUT_3_11: U9401.21
- new net DRV_OUT_3_12: U9401.28
- new net DRV_OUT_3_13: U9401.29
- new net DRV_OUT_3_14: U9401.31
- new net DRV_OUT_3_15: U9401.32
- new net DRV_OUT_3_4: U9401.12
- new net DRV_OUT_3_5: U9401.13
- new net DRV_OUT_3_6: U9401.15
- new net DRV_OUT_3_7: U9401.16
- new net DRV_OUT_3_8: U9401.17
- new net DRV_OUT_3_9: U9401.18
- new net N$10: R9621.1
- new net N$11: R9622.1
- new net N$12: R9611.2, U9601.22
- new net N$13: R9511.2, U9501.22
- new net N$14: R9623.1
- new net N$15: R9411.2, U9401.22
- new net N$16: R9624.1
- new net N$17: R9625.1
- new net N$18: R9626.1
- new net N$30: R9524.1
- new net N$31: R9424.1
- new net RELAY1: U9601.1, X9701.1
- new net RELAY10: U9601.18, X9701.10
- new net RELAY11: U9601.20, X9701.11
- new net RELAY12: U9601.21, X9701.12
- new net RELAY13: U9601.28, X9701.13
- new net RELAY14: U9601.29, X9701.14
- new net RELAY15: U9601.31, X9701.15
- new net RELAY16: U9601.32, X9701.16
- new net RELAY17: U9501.1, X9701.17
- new net RELAY18: U9501.2, X9701.18
- new net RELAY19: U9501.4, X9701.19
- new net RELAY2: U9601.2, X9701.2
- new net RELAY20: U9501.5, X9701.20
- new net RELAY21: U9501.12, X9702.1
- new net RELAY22: U9501.13, X9702.2
- new net RELAY23: U9501.15, X9702.3
- new net RELAY24: U9501.16, X9702.4
- new net RELAY25: U9501.17, X9702.5
- new net RELAY26: U9501.18, X9702.6
- new net RELAY27: U9501.20, X9702.7
- new net RELAY28: U9501.21, X9702.8
- new net RELAY29: U9501.28, X9702.9
- new net RELAY3: U9601.4, X9701.3
- new net RELAY30: U9501.29, X9702.10
- new net RELAY31: U9501.31, X9702.11
- new net RELAY32: U9501.32, X9702.12
- new net RELAY33: U9401.1, X9702.13
- new net RELAY34: U9401.2, X9702.14
- new net RELAY35: U9401.4, X9702.15
- new net RELAY36: U9401.5, X9702.16
- new net RELAY4: U9601.5, X9701.4
- new net RELAY5: U9601.12, X9701.5
- new net RELAY6: U9601.13, X9701.6
- new net RELAY7: U9601.15, X9701.7
- new net RELAY8: U9601.16, X9701.8
- new net RELAY9: U9601.17, X9701.9
- new net SPI_DRV_!RST: R9625.2, U9401.27, U9501.27, U9601.27
- new net SPI_DRV_C_!CS: R9524.2
- new net SPI_DRV_EXT_!CS: R9424.2
- new net SPI_DRV_L_!CS: R9624.2, U9401.14, U9501.14, U9601.14
- new net SPI_DRV_PWM: R9626.2, U9401.30, U9501.30, U9601.30
- new net SPI_DRV_SCLK: R9621.2, U9401.11, U9501.11, U9601.11
- new net SPI_DRV_SI: R9623.2, U9401.19, U9501.19, U9601.19
- new net SPI_DRV_SO: R9411.1, R9511.1, R9611.1, R9622.2
- new net TPS_LBI: R9001.2, R9002.1, U9001.6
- new net TPS_LBO: R9022.1, U9001.2
- new net TPS_PG: R9021.1, U9001.4
- new net TPS_SW: L9011.2, U9001.9
- net +12V: now also C9402.1, C9403.1, C9502.1, C9503.1, C9602.1, C9603.1, U9401.6, U9501.6, U9601.6
- net +3V3: now also C9011.1, C9401.2, C9501.2, C9601.2, L9011.1, R9021.2, R9022.2, U9001.5, U9401.3, U9501.3, U9601.3
- net GND: now also C9001.2, C9011.2, C9401.1, C9402.2, C9403.2, C9501.1, C9502.2, C9503.2, C9601.1, C9602.2, C9603.2, R9001.1, U9001.10, U9001.3, U9001.7, U9401.10, U9401.23, U9401.24, U9401.25, U9401.26, U9401.33, U9401.7, U9401.8, U9401.9, U9501.10, U9501.23, U9501.24, U9501.25, U9501.26, U9501.33, U9501.7, U9501.8, U9501.9, U9601.10, U9601.23, U9601.24, U9601.25, U9601.26, U9601.33, U9601.7, U9601.8, U9601.9
